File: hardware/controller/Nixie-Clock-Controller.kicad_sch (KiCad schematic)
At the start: 67 parts, among them IC1 ESP32-DEVKITC-V4, IC2 74141, J1 9/12-35V DC in, J2 Nixies-Connector, J3 Input, J4 Output, J5 LEDs, J6 power_out, Q1 MPSA42, Q10 MPSA42, Q11 MPSA42, Q12 MPSA42, Q13 MPSA42, Q14 MPSA42, Q2 MPSA92, Q3 MPSA92, Q4 MPSA92, Q5 MPSA92, Q6 MPSA92, Q7 MPSA92, Q8 MPSA92, Q9 MPSA42, SW1 on/off, SW2 in voltage select, U1 L7805, U2 L7809, U3 NCH6300HV

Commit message: Fix pin Layout again
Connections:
- net GND: now also U3.1 (GND), U3.4 (GND); no longer U3.3 (VIN), U3.5 (HV)
- net at Q2.3 (C), Q3.3 (C), Q4.3 (C)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: now also U3.5 (HV); no longer U3.4 (GND)
- net at C3.1, D2.1 (K), SW2.3 (Pin_3): now also U3.3 (VIN); no longer U3.1 (GND)
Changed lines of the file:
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@@
   (junction (at 181.61 101.6) (diameter 0) (color 0 0 0 0)
+  )
+  (junction (at 250.19 95.25) (diameter 0) (color 0 0 0 0)
   )
   (junction (at 138.43 107.95) (diameter 0) (color 0 0 0 0)
@@
     (stroke (width 0) (type default) (color 0 0 0 0))
   )
-  (wire (pts (xy 269.24 100.33) (xy 250.19 100.33))
+  (wire (pts (xy 269.24 102.87) (xy 250.19 102.87))
     (stroke (width 0) (type default) (color 0 0 0 0))
   )
@@
     (stroke (width 0) (type default) (color 0 0 0 0))
   )
+  (wire (pts (xy 261.62 95.25) (xy 261.62 96.52))
+    (stroke (width 0) (type default) (color 0 0 0 0))
+  )
   (wire (pts (xy 278.13 146.05) (xy 270.51 146.05))
     (stroke (width 0) (type default) (color 0 0 0 0))
@@
     (stroke (width 0) (type default) (color 0 0 0 0))
   )
-  (wire (pts (xy 227.33 105.41) (xy 227.33 110.49))
-    (stroke (width 0) (type default) (color 0 0 0 0))
-  )
   (wire (pts (xy 152.4 95.25) (xy 152.4 99.06))
     (stroke (width 0) (type default) (color 0 0 0 0))
   )
-  (wire (pts (xy 269.24 109.22) (xy 269.24 100.33))
+  (wire (pts (xy 269.24 109.22) (xy 269.24 102.87))
     (stroke (width 0) (type default) (color 0 0 0 0))
   )
@@
     (stroke (width 0) (type default) (color 0 0 0 0))
   )
+  (wire (pts (xy 250.19 95.25) (xy 261.62 95.25))
+    (stroke (width 0) (type default) (color 0 0 0 0))
+  )
   (wire (pts (xy 91.44 90.17) (xy 91.44 69.85))
     (stroke (width 0) (type default) (color 0 0 0 0))
@@
     (stroke (width 0) (type default) (color 0 0 0 0))
   )
+  (wire (pts (xy 232.41 95.25) (xy 250.19 95.25))
+    (stroke (width 0) (type default) (color 0 0 0 0))
+  )
   (wire (pts (xy 50.8 127) (xy 45.72 127))
     (stroke (width 0) (type default) (color 0 0 0 0))
@@
     (stroke (width 0) (type default) (color 0 0 0 0))
   )
-  (wire (pts (xy 232.41 100.33) (xy 227.33 100.33))
-    (stroke (width 0) (type default) (color 0 0 0 0))
-  )
   (wire (pts (xy 181.61 40.64) (xy 181.61 76.2))
     (stroke (width 0) (type default) (color 0 0 0 0))
@@
     (stroke (width 0) (type default) (color 0 0 0 0))
   )
+  (wire (pts (xy 232.41 100.33) (xy 232.41 95.25))
+    (stroke (width 0) (type default) (color 0 0 0 0))
+  )
   (wire (pts (xy 109.22 35.56) (xy 110.49 35.56))
     (stroke (width 0) (type default) (color 0 0 0 0))
@@
     (stroke (width 0) (type default) (color 0 0 0 0))
   )
-  (wire (pts (xy 227.33 105.41) (xy 232.41 105.41))
-    (stroke (width 0) (type default) (color 0 0 0 0))
-  )
   (wire (pts (xy 156.21 15.24) (xy 156.21 21.59))
     (stroke (width 0) (type default) (color 0 0 0 0))
@@
     (stroke (width 0) (type default) (color 0 0 0 0))
   )
-  (wire (pts (xy 250.19 102.87) (xy 257.81 102.87))
-    (stroke (width 0) (type default) (color 0 0 0 0))
-  )
   (wire (pts (xy 270.51 124.46) (xy 251.46 124.46))
     (stroke (width 0) (type default) (color 0 0 0 0))
@@
     (stroke (width 0) (type default) (color 0 0 0 0))
   )
+  (wire (pts (xy 250.19 95.25) (xy 250.19 100.33))
+    (stroke (width 0) (type default) (color 0 0 0 0))
+  )
   (wire (pts (xy 148.59 158.75) (xy 148.59 147.32))
     (stroke (width 0) (type default) (color 0 0 0 0))
@@
     (stroke (width 0) (type default) (color 0 0 0 0))
   )
-  (wire (pts (xy 214.63 97.79) (xy 214.63 57.15))
+  (wire (pts (xy 214.63 105.41) (xy 214.63 57.15))
     (stroke (width 0) (type default) (color 0 0 0 0))
   )
@@
     (stroke (width 0) (type default) (color 0 0 0 0))
   )
-  (wire (pts (xy 214.63 97.79) (xy 227.33 97.79))
+  (wire (pts (xy 214.63 105.41) (xy 232.41 105.41))
     (stroke (width 0) (type default) (color 0 0 0 0))
   )
@@
   )
   (wire (pts (xy 66.04 127) (xy 66.04 134.62))
-    (stroke (width 0) (type default) (color 0 0 0 0))
-  )
-  (wire (pts (xy 227.33 97.79) (xy 227.33 100.33))
     (stroke (width 0) (type default) (color 0 0 0 0))
   )
@@
     (pin "3")
   )
-  (symbol (lib_id "power:GND") (at 227.33 110.49 0) (unit 1)
-    (in_bom yes) (on_board yes)
-    (property "Reference" "#PWR013" (id 0) (at 227.33 116.84 0)
-      (effects (font (size 1.27 1.27)) hide)
-    )
-    (property "Value" "GND" (id 1) (at 227.457 114.8842 0))
-    (property "Footprint" "" (id 2) (at 227.33 110.49 0)
-      (effects (font (size 1.27 1.27)) hide)
-    )
-    (property "Datasheet" "" (id 3) (at 227.33 110.49 0)
-      (effects (font (size 1.27 1.27)) hide)
-    )
-    (pin "1")
-  )
   (symbol (lib_id "Connector:Screw_Terminal_01x02") (at 224.79 85.09 180) (unit 1)
     (in_bom yes) (on_board yes)
@@
     (pin "2")
   )
-  (symbol (lib_id "power:GND") (at 257.81 102.87 0) (unit 1)
-    (in_bom yes) (on_board yes)
-    (property "Reference" "#PWR0102" (id 0) (at 257.81 109.22 0)
-      (effects (font (size 1.27 1.27)) hide)
-    )
-    (property "Value" "GND" (id 1) (at 257.937 107.2642 0))
-    (property "Footprint" "" (id 2) (at 257.81 102.87 0)
-      (effects (font (size 1.27 1.27)) hide)
-    )
-    (property "Datasheet" "" (id 3) (at 257.81 102.87 0)
+  (symbol (lib_id "power:GND") (at 261.62 96.52 0) (unit 1)
+    (in_bom yes) (on_board yes)
+    (property "Reference" "#PWR0102" (id 0) (at 261.62 102.87 0)
+      (effects (font (size 1.27 1.27)) hide)
+    )
+    (property "Value" "GND" (id 1) (at 261.747 100.9142 0))
+    (property "Footprint" "" (id 2) (at 261.62 96.52 0)
+      (effects (font (size 1.27 1.27)) hide)
+    )
+    (property "Datasheet" "" (id 3) (at 261.62 96.52 0)
       (effects (font (size 1.27 1.27)) hide)
     )
@@
       (reference "#PWR011") (unit 1) (value "GND") (footprint "")
     )
-    (path "/00000000-0000-0000-0000-000061d798c4"
-      (reference "#PWR013") (unit 1) (value "GND") (footprint "")
-    )
     (path "/00000000-0000-0000-0000-0000619bfd9f"

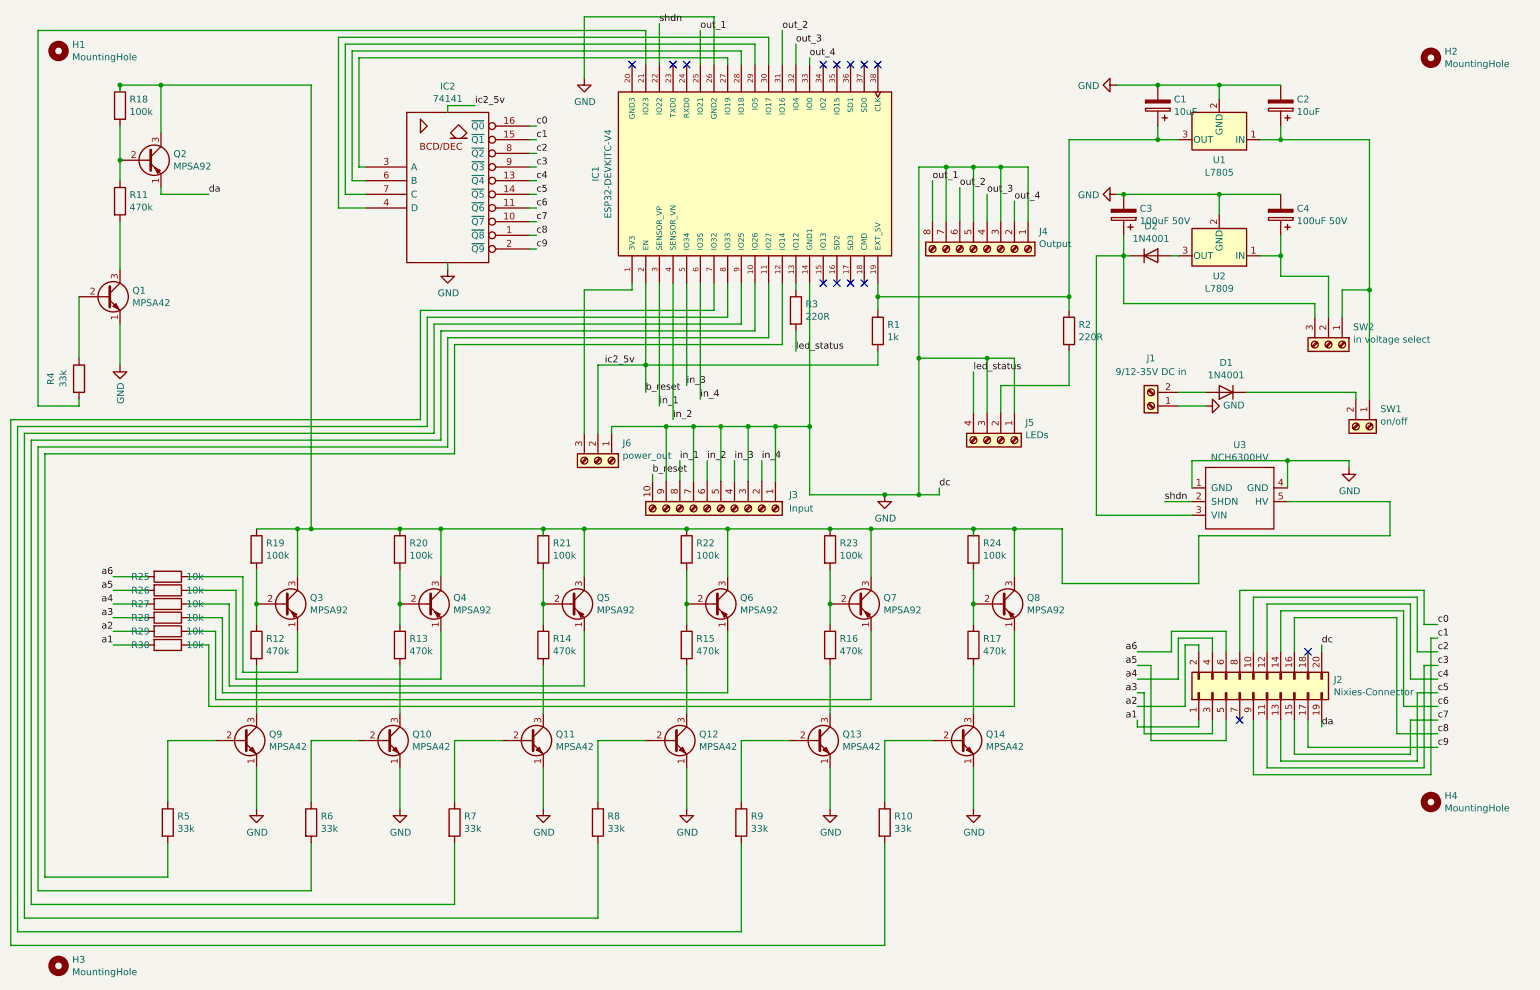
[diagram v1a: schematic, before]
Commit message: fix wrong transistor connections
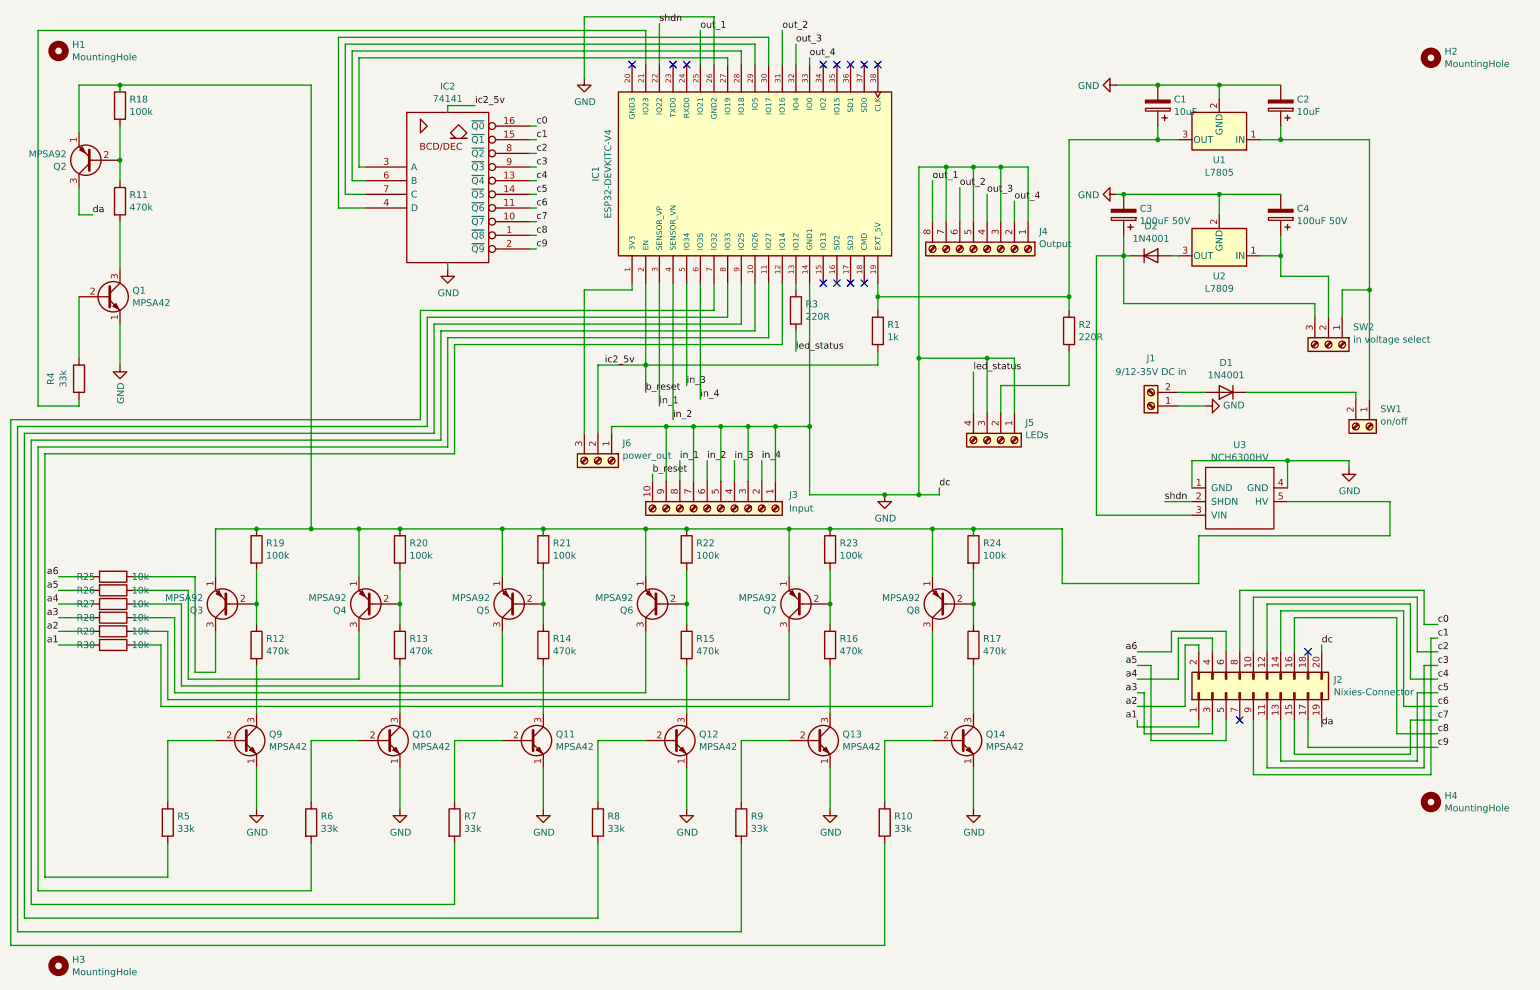
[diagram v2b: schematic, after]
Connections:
- net da: now also Q2.3 (C); no longer Q2.1 (E)
- net at Q3.1 (E): now also Q2.1 (E), Q4.1 (E), Q5.1 (E), Q6.1 (E), Q7.1 (E), Q8.1 (E), R18.1, R19.1, R20.1, R21.1, R22.1, R23.1, R24.1, U3.5 (HV); no longer R25.1
- net at R26.1: now also Q4.3 (C); no longer Q4.1 (E)
- net at R27.1: now also Q5.3 (C); no longer Q5.1 (E)
- net at R28.1: now also Q6.3 (C); no longer Q6.1 (E)
- net at R29.1: now also Q7.3 (C); no longer Q7.1 (E)
- net at R30.1: now also Q8.3 (C); no longer Q8.1 (E)
- new net: Q3.3 (C), R25.1
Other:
- moved on the sheet: Q2, Q3, Q4, Q5, Q6, Q7, Q8, R25, R26, R27, R28, R29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

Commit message: Improve transistor numbering
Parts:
- renumbered Q3 to Q1, Q11 to Q10, Q12 to Q11, Q13 to Q12, Q14 to Q13, Q1 to Q14, Q4 to Q2, Q5 to Q3, Q6 to Q4, Q7 to Q5, Q8 to Q6, Q2 to Q7, Q9 to Q8, Q10 to Q9
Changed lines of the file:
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@@
   (symbol (lib_id "Transistor_BJT:MPSA42") (at 55.88 147.32 0) (unit 1)
     (in_bom yes) (on_board yes)
-    (property "Reference" "Q9" (id 0) (at 60.7314 146.1516 0)
+    (property "Reference" "Q8" (id 0) (at 60.7314 146.1516 0)
       (effects (font (size 1.27 1.27)) (justify left))
     )
@@
   (symbol (lib_id "Transistor_BJT:MPSA42") (at 82.55 147.32 0) (unit 1)
     (in_bom yes) (on_board yes)
-    (property "Reference" "Q10" (id 0) (at 87.4014 146.1516 0)
+    (property "Reference" "Q9" (id 0) (at 87.4014 146.1516 0)
       (effects (font (size 1.27 1.27)) (justify left))
     )
@@
   (symbol (lib_id "Transistor_BJT:MPSA42") (at 109.22 147.32 0) (unit 1)
     (in_bom yes) (on_board yes)
-    (property "Reference" "Q11" (id 0) (at 114.0714 146.1516 0)
+    (property "Reference" "Q10" (id 0) (at 114.0714 146.1516 0)
       (effects (font (size 1.27 1.27)) (justify left))
     )
@@
   (symbol (lib_id "Transistor_BJT:MPSA42") (at 135.89 147.32 0) (unit 1)
     (in_bom yes) (on_board yes)
-    (property "Reference" "Q12" (id 0) (at 140.7414 146.1516 0)
+    (property "Reference" "Q11" (id 0) (at 140.7414 146.1516 0)
       (effects (font (size 1.27 1.27)) (justify left))
     )
@@
   (symbol (lib_id "Transistor_BJT:MPSA42") (at 162.56 147.32 0) (unit 1)
     (in_bom yes) (on_board yes)
-    (property "Reference" "Q13" (id 0) (at 167.4114 146.1516 0)
+    (property "Reference" "Q12" (id 0) (at 167.4114 146.1516 0)
       (effects (font (size 1.27 1.27)) (justify left))
     )
@@
   (symbol (lib_id "Transistor_BJT:MPSA42") (at 189.23 147.32 0) (unit 1)
     (in_bom yes) (on_board yes)
-    (property "Reference" "Q14" (id 0) (at 194.0814 146.1516 0)
+    (property "Reference" "Q13" (id 0) (at 194.0814 146.1516 0)
       (effects (font (size 1.27 1.27)) (justify left))
     )
@@
   (symbol (lib_id "Transistor_BJT:MPSA92") (at 53.34 121.92 180) (unit 1)
     (in_bom yes) (on_board yes)
-    (property "Reference" "Q3" (id 0) (at 48.4886 123.0884 0)
+    (property "Reference" "Q1" (id 0) (at 48.4886 123.0884 0)
       (effects (font (size 1.27 1.27)) (justify left))
     )
@@
   (symbol (lib_id "Transistor_BJT:MPSA92") (at 80.01 121.92 180) (unit 1)
     (in_bom yes) (on_board yes)
-    (property "Reference" "Q4" (id 0) (at 75.1586 123.0884 0)
+    (property "Reference" "Q2" (id 0) (at 75.1586 123.0884 0)
       (effects (font (size 1.27 1.27)) (justify left))
     )
@@
   (symbol (lib_id "Transistor_BJT:MPSA92") (at 106.68 121.92 180) (unit 1)
     (in_bom yes) (on_board yes)
-    (property "Reference" "Q5" (id 0) (at 101.8286 123.0884 0)
+    (property "Reference" "Q3" (id 0) (at 101.8286 123.0884 0)
       (effects (font (size 1.27 1.27)) (justify left))
     )
@@
   (symbol (lib_id "Transistor_BJT:MPSA92") (at 133.35 121.92 180) (unit 1)
     (in_bom yes) (on_board yes)
-    (property "Reference" "Q6" (id 0) (at 128.4986 123.0884 0)
+    (property "Reference" "Q4" (id 0) (at 128.4986 123.0884 0)
       (effects (font (size 1.27 1.27)) (justify left))
     )
@@
   (symbol (lib_id "Transistor_BJT:MPSA92") (at 160.02 121.92 180) (unit 1)
     (in_bom yes) (on_board yes)
-    (property "Reference" "Q7" (id 0) (at 155.1686 123.0884 0)
+    (property "Reference" "Q5" (id 0) (at 155.1686 123.0884 0)
       (effects (font (size 1.27 1.27)) (justify left))
     )
@@
   (symbol (lib_id "Transistor_BJT:MPSA92") (at 186.69 121.92 180) (unit 1)
     (in_bom yes) (on_board yes)
-    (property "Reference" "Q8" (id 0) (at 181.8386 123.0884 0)
+    (property "Reference" "Q6" (id 0) (at 181.8386 123.0884 0)
       (effects (font (size 1.27 1.27)) (justify left))
     )
@@
   (symbol (lib_id "Transistor_BJT:MPSA42") (at 30.48 64.77 0) (unit 1)
     (in_bom yes) (on_board yes)
-    (property "Reference" "Q1" (id 0) (at 35.3314 63.6016 0)
+    (property "Reference" "Q14" (id 0) (at 35.3314 63.6016 0)
       (effects (font (size 1.27 1.27)) (justify left))
     )
@@
   (symbol (lib_id "Transistor_BJT:MPSA92") (at 27.94 39.37 180) (unit 1)
     (in_bom yes) (on_board yes)
-    (property "Reference" "Q2" (id 0) (at 23.0886 40.5384 0)
+    (property "Reference" "Q7" (id 0) (at 23.0886 40.5384 0)
       (effects (font (size 1.27 1.27)) (justify left))
     )
@@
       (reference "J6") (unit 1) (value "power_out") (footprint "TerminalBlock_RND:TerminalBlock_RND_205-00013_1x03_P5.00mm_Horizontal")
     )
+    (path "/00000000-0000-0000-0000-00006189e5ed"
+      (reference "Q1") (unit 1) (value "MPSA92") (footprint "Package_TO_SOT_THT:TO-92_Inline")
+    )
+    (path "/00000000-0000-0000-0000-0000618a5945"
+      (reference "Q2") (unit 1) (value "MPSA92") (footprint "Package_TO_SOT_THT:TO-92_Inline")
+    )
+    (path "/00000000-0000-0000-0000-0000618a73d7"
+      (reference "Q3") (unit 1) (value "MPSA92") (footprint "Package_TO_SOT_THT:TO-92_Inline")
+    )
+    (path "/00000000-0000-0000-0000-0000618a8c2c"
+      (reference "Q4") (unit 1) (value "MPSA92") (footprint "Package_TO_SOT_THT:TO-92_Inline")
+    )
+    (path "/00000000-0000-0000-0000-0000618aa58f"
+      (reference "Q5") (unit 1) (value "MPSA92") (footprint "Package_TO_SOT_THT:TO-92_Inline")
+    )
+    (path "/00000000-0000-0000-0000-0000618af917"
+      (reference "Q6") (unit 1) (value "MPSA92") (footprint "Package_TO_SOT_THT:TO-92_Inline")
+    )
+    (path "/00000000-0000-0000-0000-0000619f1f00"
+      (reference "Q7") (unit 1) (value "MPSA92") (footprint "Package_TO_SOT_THT:TO-92_Inline")
+    )
+    (path "/00000000-0000-0000-0000-0000618901be"
+      (reference "Q8") (unit 1) (value "MPSA42") (footprint "Package_TO_SOT_THT:TO-92_Inline")
+    )
+    (path "/00000000-0000-0000-0000-0000618951fd"
+      (reference "Q9") (unit 1) (value "MPSA42") (footprint "Package_TO_SOT_THT:TO-92_Inline")
+    )
+    (path "/00000000-0000-0000-0000-000061897a75"
+      (reference "Q10") (unit 1) (value "MPSA42") (footprint "Package_TO_SOT_THT:TO-92_Inline")
+    )
+    (path "/00000000-0000-0000-0000-000061898fdb"
+      (reference "Q11") (unit 1) (value "MPSA42") (footprint "Package_TO_SOT_THT:TO-92_Inline")
+    )
+    (path "/00000000-0000-0000-0000-000061899134"
+      (reference "Q12") (unit 1) (value "MPSA42") (footprint "Package_TO_SOT_THT:TO-92_Inline")
+    )
+    (path "/00000000-0000-0000-0000-000061899155"
+      (reference "Q13") (unit 1) (value "MPSA42") (footprint "Package_TO_SOT_THT:TO-92_Inline")
+    )
     (path "/00000000-0000-0000-0000-0000619f057a"
-      (reference "Q1") (unit 1) (value "MPSA42") (footprint "Package_TO_SOT_THT:TO-92_Inline")
-    )
-    (path "/00000000-0000-0000-0000-0000619f1f00"
-      (reference "Q2") (unit 1) (value "MPSA92") (footprint "Package_TO_SOT_THT:TO-92_Inline")
-    )
-    (path "/00000000-0000-0000-0000-00006189e5ed"
-      (reference "Q3") (unit 1) (value "MPSA92") (footprint "Package_TO_SOT_THT:TO-92_Inline")
-    )
-    (path "/00000000-0000-0000-0000-0000618a5945"
-      (reference "Q4") (unit 1) (value "MPSA92") (footprint "Package_TO_SOT_THT:TO-92_Inline")
-    )
-    (path "/00000000-0000-0000-0000-0000618a73d7"
-      (reference "Q5") (unit 1) (value "MPSA92") (footprint "Package_TO_SOT_THT:TO-92_Inline")
-    )
-    (path "/00000000-0000-0000-0000-0000618a8c2c"
-      (reference "Q6") (unit 1) (value "MPSA92") (footprint "Package_TO_SOT_THT:TO-92_Inline")
-    )
-    (path "/00000000-0000-0000-0000-0000618aa58f"
-      (reference "Q7") (unit 1) (value "MPSA92") (footprint "Package_TO_SOT_THT:TO-92_Inline")
-    )
-    (path "/00000000-0000-0000-0000-0000618af917"
-      (reference "Q8") (unit 1) (value "MPSA92") (footprint "Package_TO_SOT_THT:TO-92_Inline")
-    )
-    (path "/00000000-0000-0000-0000-0000618901be"
-      (reference "Q9") (unit 1) (value "MPSA42") (footprint "Package_TO_SOT_THT:TO-92_Inline")
-    )
-    (path "/00000000-0000-0000-0000-0000618951fd"
-      (reference "Q10") (unit 1) (value "MPSA42") (footprint "Package_TO_SOT_THT:TO-92_Inline")
-    )
-    (path "/00000000-0000-0000-0000-000061897a75"
-      (reference "Q11") (unit 1) (value "MPSA42") (footprint "Package_TO_SOT_THT:TO-92_Inline")
-    )
-    (path "/00000000-0000-0000-0000-000061898fdb"
-      (reference "Q12") (unit 1) (value "MPSA42") (footprint "Package_TO_SOT_THT:TO-92_Inline")
-    )
-    (path "/00000000-0000-0000-0000-000061899134"
-      (reference "Q13") (unit 1) (value "MPSA42") (footprint "Package_TO_SOT_THT:TO-92_Inline")
-    )
-    (path "/00000000-0000-0000-0000-000061899155"
       (reference "Q14") (unit 1) (value "MPSA42") (footprint "Package_TO_SOT_THT:TO-92_Inline")
     )
